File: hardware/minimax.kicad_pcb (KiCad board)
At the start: 2 copper layers, 25 x 35 mm, 35 parts, among them J1 524352271, J2 2FA1-NZSP-PCBB6, U1 MAX96717GTJ/VY+

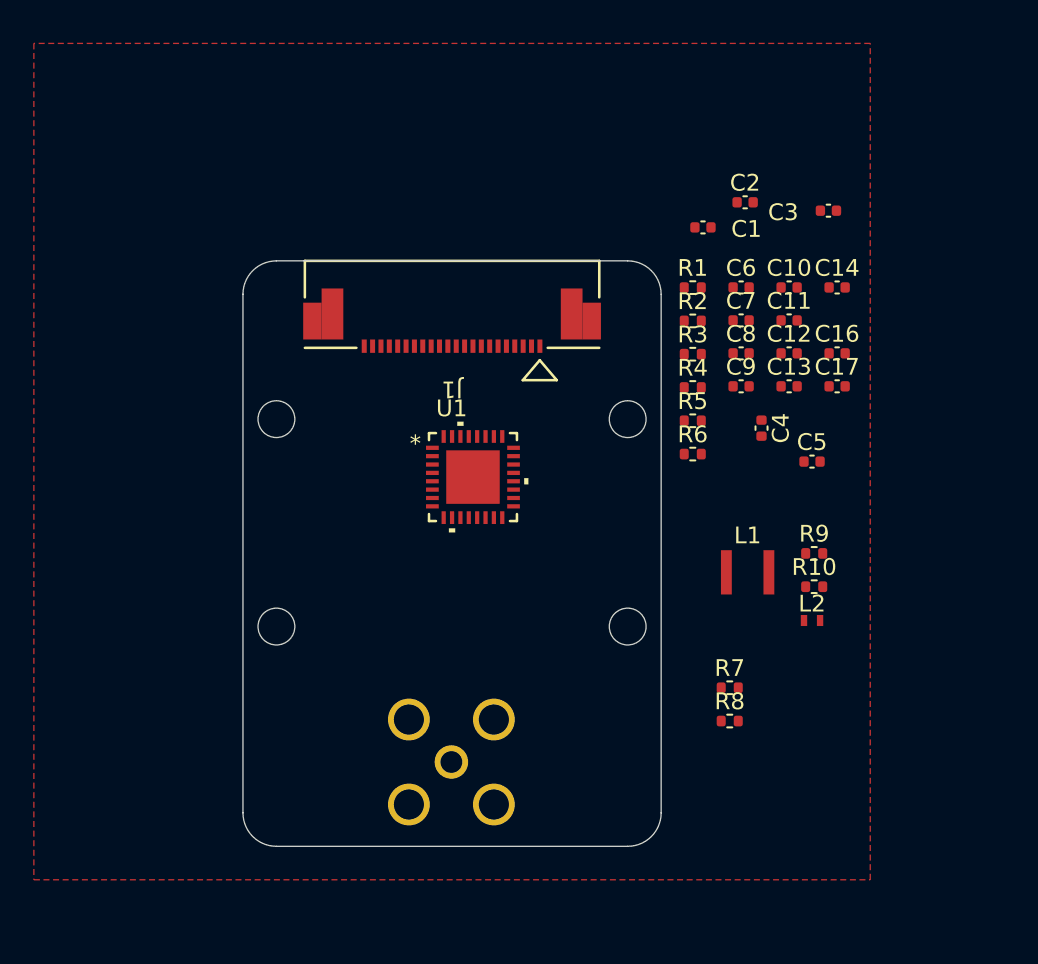
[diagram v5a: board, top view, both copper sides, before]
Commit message: started power, added smt fakra
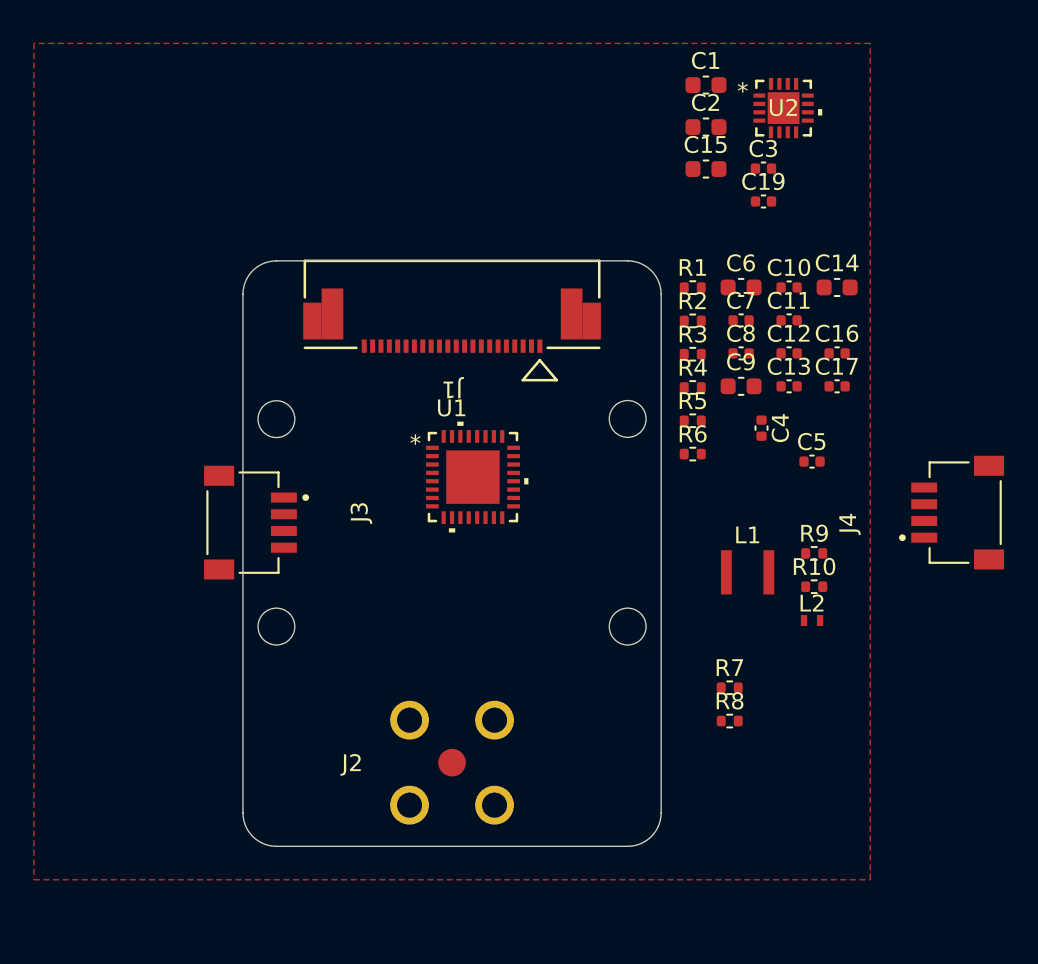
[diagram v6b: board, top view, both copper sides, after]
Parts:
- removed REF** (x4): MountingHole_2.2mm_M2, MountingHole:MountingHole_2.2mm_M2
- added C15: 10U, Capacitor_SMD:C_0603_1608Metric, F.Cu at (165.2, 82.5)
- added C19: 100N, Capacitor_SMD:C_0402_1005Metric, F.Cu at (168.6, 84.5)
- added H1: MountingHole, MountingHole:MountingHole_2.2mm_M2, F.Cu at (139.5, 97.5)
- added H2: MountingHole, MountingHole:MountingHole_2.2mm_M2, F.Cu at (160.5, 97.5)
- added H3: MountingHole, MountingHole:MountingHole_2.2mm_M2, F.Cu at (139.5, 109.9)
- added H4: MountingHole, MountingHole:MountingHole_2.2mm_M2, F.Cu at (160.5, 109.9)
- added J3: PRT-14417, user:SPARKFUN_PRT-14417, F.Cu at (137.5, 103.7)
- added J4: PRT-14417, user:SPARKFUN_PRT-14417, F.Cu at (180.7, 103.0)
- added U2: MAX20049ATED/VY+, user:21-100150D_T1633Y&plus_5C_MXM, F.Cu at (169.8, 78.9)
- C1, C2: value 1U -> 10U; footprint Capacitor_SMD:C_0402_1005Metric -> Capacitor_SMD:C_0603_1608Metric
- C14, C6, C9: footprint Capacitor_SMD:C_0402_1005Metric -> Capacitor_SMD:C_0603_1608Metric
- C3: value 1U -> 100N
- J2: footprint user:2FA1-NZSP-PCBB6 -> user:59S1AC-40MT5-Z; moved to F.Cu
- moved C1 8.51 mm to (165.2, 77.5)
- moved C2 5.07 mm to (165.2, 80.0)
- moved C3 4.63 mm to (168.6, 82.5)
- moved J2 0.06 mm to (150.0, 118.0), turned to 0 degrees
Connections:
- C1 pad 1: +1V8 -> /connector/V_POC
- C14 pad 1: unconnected-(C14-Pad1) -> Net-(U2-OUTS3)
- C2 pad 1: +1V2 -> /connector/V_POC
- C3 pad 1: +2V8 -> Net-(U2-LX2)
- C3 pad 2: GND -> Net-(U2-BST2)
- C6 pad 1: unconnected-(C6-Pad1) -> +1V2
- C9 pad 1: unconnected-(C9-Pad1) -> +1V8

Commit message: finished schematic, changed to 4 layer board
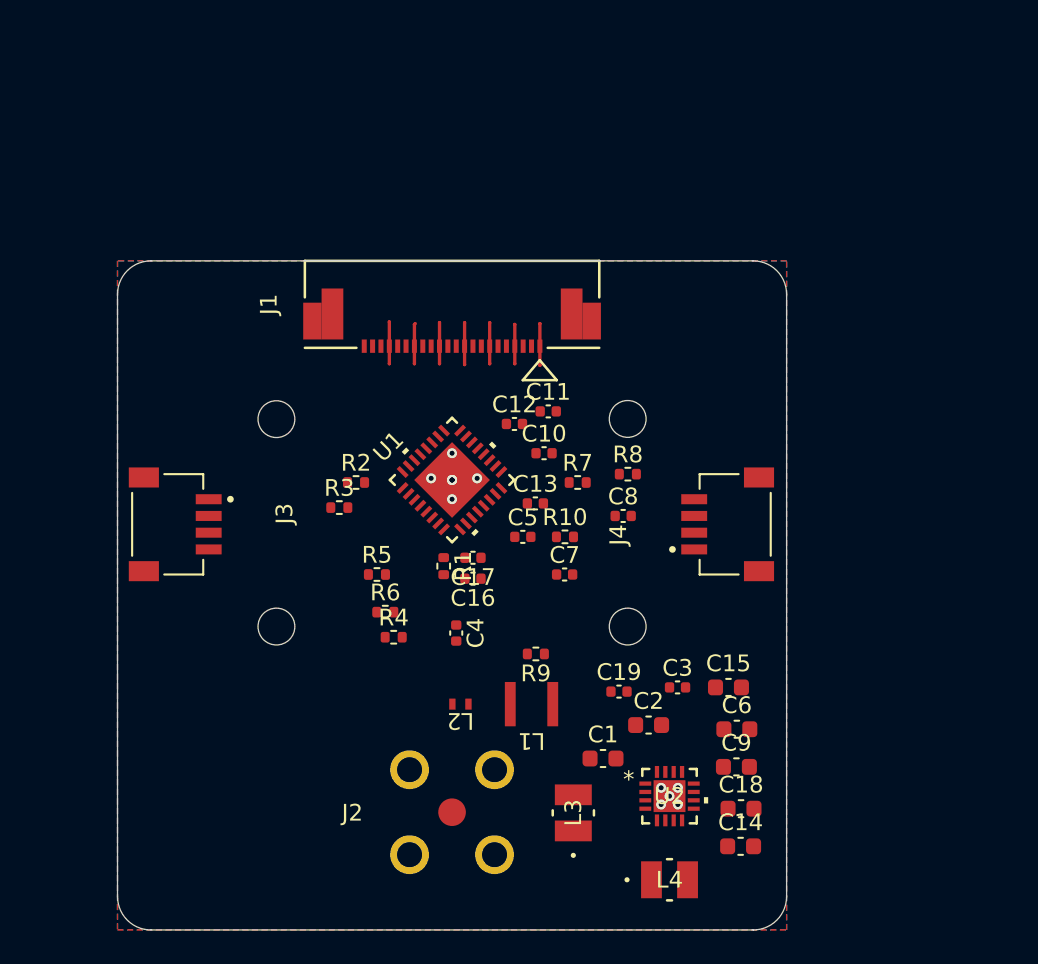
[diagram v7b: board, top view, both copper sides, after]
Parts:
- added C18: 10U, Capacitor_SMD:C_0603_1608Metric, F.Cu at (167.3, 120.8)
- added L3: 3U3, user:IND_TFM252012ALMA_TDK, F.Cu at (157.2, 121.0)
- added L4: 3U3, user:IND_TFM252012ALMA_TDK, F.Cu at (163.0, 125.0)
- L1: value PFL1005-561MRW -> 1210POC-223MRC
- moved U2 41.7 mm to (163.0, 120.0)
- moved C1 40.7 mm to (159.0, 117.8)
- moved C2 35.9 mm to (161.8, 115.8)
- moved C14 33.9 mm to (167.2, 123.0)
- moved C3 31.4 mm to (163.5, 113.5)
- moved C15 31.0 mm to (166.5, 113.5)
- moved C19 30.5 mm to (160.0, 113.8)
- moved C6 26.4 mm to (167.0, 116.0)
- moved C16 25.6 mm to (151.2, 107.0), turned to 180 degrees
- moved C17 24.1 mm to (151.2, 105.8), turned to 180 degrees
- moved R4 23.3 mm to (146.5, 110.5)
- moved R3 23.0 mm to (143.3, 102.8)
- moved C9 22.8 mm to (167.0, 118.2)
- moved R1 22.3 mm to (149.5, 106.2), turned to -90 degrees
- moved R2 22.3 mm to (144.3, 101.2)
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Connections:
- U1 pad 18: MFP4 -> /camera/LED_EN
- U1 pad 19: /camera/MIPI.CSI_D2_P -> /camera/MIPI.CSI_D0_N
- U1 pad 2: MFP0 -> /camera/POWER_EN
- U1 pad 20: /camera/MIPI.CSI_D2_N -> /camera/MIPI.CSI_D0_P
- U1 pad 23: /camera/MIPI.CSI_D3_P -> /camera/MIPI.CSI_D1_N
- U1 pad 24: /camera/MIPI.CSI_D3_N -> /camera/MIPI.CSI_D1_P
- U1 pad 25: /camera/MIPI.CSI_D0_P -> /camera/MIPI.CSI_D2_N
- U1 pad 26: /camera/MIPI.CSI_D0_N -> /camera/MIPI.CSI_D2_P
- U1 pad 27: /camera/MIPI.CSI_CLK_P -> /camera/MIPI.CSI_CLK_N
- U1 pad 28: /camera/MIPI.CSI_CLK_N -> /camera/MIPI.CSI_CLK_P
- U1 pad 29: /camera/MIPI.CSI_D1_P -> /camera/MIPI.CSI_D3_N
- U1 pad 30: /camera/MIPI.CSI_D1_N -> /camera/MIPI.CSI_D3_P
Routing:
- net GND: track 0.00 -> 17.2 mm, vias 0 -> 11
- added copper zone on B.Cu, net GND
- added copper zone on In1.Cu, net GND
- added copper zone on In2.Cu, net GND
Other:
- board size 25 x 35 mm -> 40 x 40 mm
- copper layers 2 -> 4
- rule pad_to_mask_clearance: 0 -> 0.0508

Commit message: layout planning and decided to use bottom layer for components
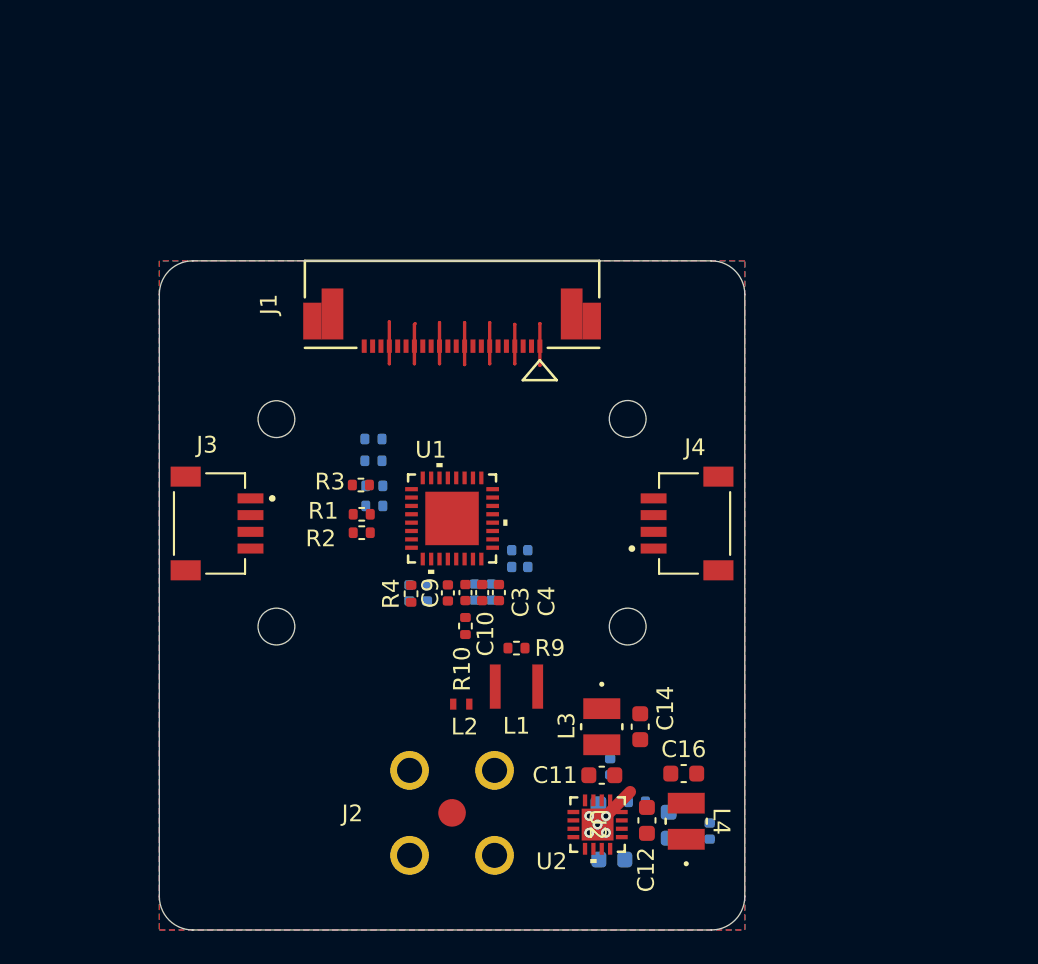
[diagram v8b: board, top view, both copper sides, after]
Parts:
- added R11: 5.1K, Resistor_SMD:R_0402_1005Metric, B.Cu at (161.1, 120.3)
- C1: renamed from C16; moved to B.Cu
- C13: renamed from C3; moved to B.Cu
- C15: renamed from C19; moved to B.Cu
- C17: renamed from C15; moved to B.Cu
- C18: renamed from C6; moved to B.Cu
- C19: renamed from C14; moved to B.Cu
- C2: renamed from C17; moved to B.Cu
- C5: renamed from C10; moved to B.Cu
- C6: renamed from C11; moved to B.Cu
- C7, C8: moved to B.Cu
- R5: renamed from R3; moved to B.Cu
- R6: renamed from R5; moved to B.Cu
- R7: renamed from R4; moved to B.Cu
- R8: renamed from R6; moved to B.Cu
- moved R2 16.3 mm to (144.6, 104.2)
- moved R1 13.0 mm to (144.6, 103.2)
- moved C6 11.3 mm to (152.3, 107.8), turned to -90 degrees
- moved R7 10.6 mm to (145.3, 100.0), turned to 180 degrees
- moved C3 10.3 mm to (151.8, 107.8), turned to -90 degrees
- moved C15 9.95 mm to (165.4, 122.1), turned to 90 degrees
- moved C18 9.79 mm to (158.8, 121.2), turned to 90 degrees
- moved C5 9.28 mm to (151.3, 107.8), turned to -90 degrees
- moved C17 8.98 mm to (162.9, 121.7), turned to 90 degrees
- moved R10 7.99 mm to (150.8, 109.8), turned to -90 degrees
- moved C19 7.74 mm to (159.6, 123.8)
- moved R8 7.58 mm to (145.3, 101.5), turned to 180 degrees
- moved C8 6.89 mm to (154.1, 106.3)
- moved C14 6.23 mm to (161.2, 115.8), turned to -90 degrees
- moved C13 6.22 mm to (159.4, 118.2), turned to -90 degrees
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- renumbered C5 to C10, C1 to C11, C2 to C12, C9 to C14, C18 to C16, C12 to C3, C13 to C4, C4 to C9, R7 to R1, R8 to R2, R2 to R3, R1 to R4
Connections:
- U2 pad 5: unconnected-(U2-PGOOD-Pad5) -> Net-(U2-PGOOD)
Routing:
- net GND: track 17.2 -> 19.9 mm, vias 11 -> 5
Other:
- board size 40 x 40 mm -> 35 x 40 mm
- board text added: "Layer Name Function 1 F.Cu Signal 2 In1.Cu GND (Controlled Impedance) 3 In1.Cu Power 4 B.Cu GND"
